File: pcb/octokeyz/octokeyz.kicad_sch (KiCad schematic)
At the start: 29 parts, among them J1 USB, J2 ISP Programming, SW1 SW_Push, SW2 SW_Push, SW3 SW_Push, SW4 SW_Push, SW5 SW_Push, SW6 SW_Push, SW7 SW_Push, SW8 SW_Push, U1 ATtiny4313-P, Y1 20MHz

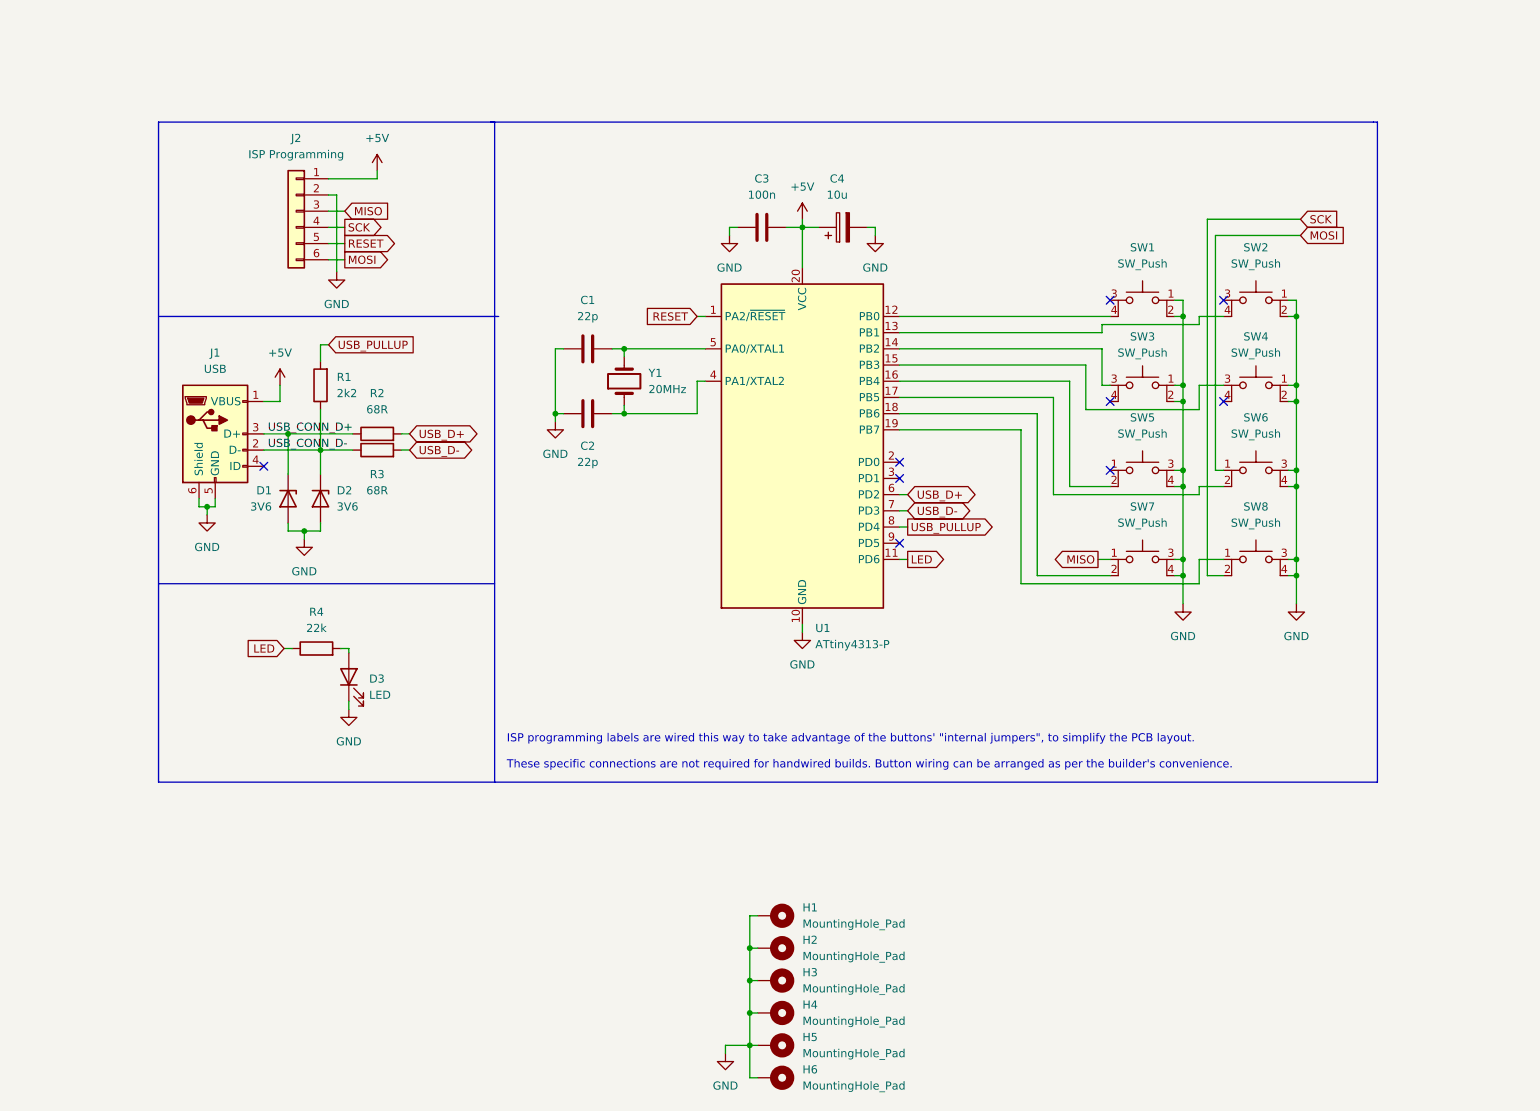
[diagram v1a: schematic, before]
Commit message: pcb: octokeyz: revision 20240616
use stm32 instead of avr microcontroller. the prices are similar
nowadays, and it will allow us to have a single DFU-capable and
BSD-licensed firmware usable by all boards.

the board outline and the position of buttons and connectors is the
same, any existing cases should still fit correctly.
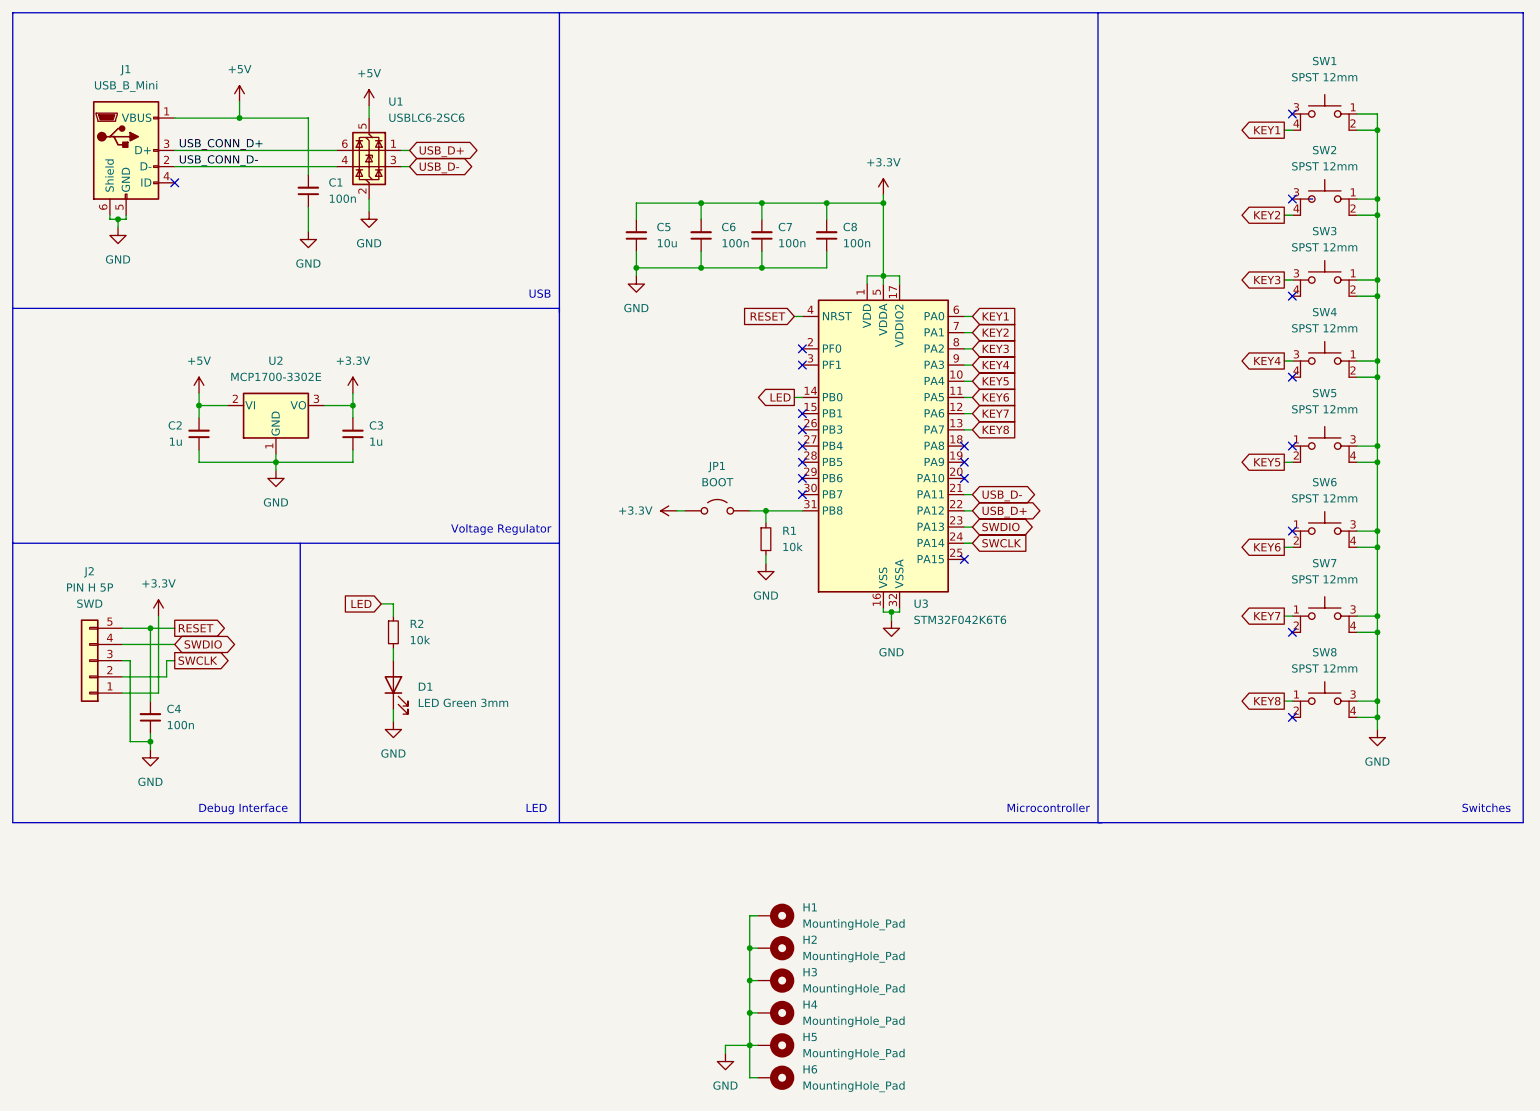
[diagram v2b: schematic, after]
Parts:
- removed C1, C2: 22p, Capacitor_THT:C_Disc_D3.0mm_W1.6mm_P2.50mm, symbol Device:C
- removed C3: 100n, octokeyz:C_TDK_FA28, symbol Device:C
- removed C4: 10u, octokeyz:CP_Radial_D5.0mm_P2.50mm_Horizontal, symbol Device:C_Polarized
- removed D1, D2: 3V6, Diode_THT:D_DO-35_SOD27_P7.62mm_Horizontal, symbol Device:D_Zener
- removed D3: LED, LED_THT:LED_D3.0mm, symbol Device:LED
- removed J2: ISP Programming, Connector_PinHeader_2.54mm:PinHeader_1x06_P2.54mm_Horizontal, symbol Connector_Generic:Conn_01x06
- removed R1: 2k2, octokeyz:R_YAGEO_MFR-25FTE52_Horizontal, symbol Device:R
- removed R2, R3: 68R, octokeyz:R_YAGEO_MFR-25FTE52_Horizontal, symbol Device:R
- removed R4: 22k, octokeyz:R_YAGEO_MFR-25FTE52_Horizontal, symbol Device:R
- removed U1: ATtiny4313-P, Package_DIP:DIP-20_W7.62mm, symbol MCU_Microchip_ATtiny:ATtiny4313-P
- removed Y1: 20MHz, Crystal:Crystal_HC49-4H_Vertical, symbol Device:Crystal
- added C1, C4, C6, C7, C8: 100n, octokeyz:C_TDK_FA28, symbol Device:C_Small
- added C2, C3: 1u, octokeyz:C_TDK_FA28, symbol Device:C_Small
- added C5: 10u, octokeyz:C_TDK_FA26, symbol Device:C_Small
- added D1: LED Green 3mm, LED_THT:LED_D3.0mm, symbol Device:LED
- added J2: PIN H 5P, Connector_PinHeader_2.54mm:PinHeader_1x05_P2.54mm_Horizontal, symbol Connector_Generic:Conn_01x05
- added JP1: BOOT, Connector_PinHeader_2.54mm:PinHeader_1x02_P2.54mm_Horizontal, symbol Jumper:Jumper_2_Open
- added R1, R2: 10k, octokeyz:R_YAGEO_MFR-25FTE52_Horizontal, symbol Device:R_Small
- added U1: USBLC6-2SC6, Package_TO_SOT_SMD:SOT-23-6, symbol Power_Protection:USBLC6-2SC6
- added U2: MCP1700-3302E, Package_TO_SOT_THT:TO-92_Inline_Wide, symbol Regulator_Linear:MCP1700x-330xxTO
- added U3: STM32F042K6T6, Package_QFP:LQFP-32_7x7mm_P0.8mm, symbol MCU_ST_STM32F0:STM32F042K6Tx
- J1: value USB -> USB_B_Mini; MPN (none) -> GMSB0522132EU
- SW1, SW2, SW3, SW4, SW5, SW6, SW7, SW8: value SW_Push -> SPST 12mm
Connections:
- net +5V: now also C1.2, C2.2, U1.5 (VBUS), U2.2 (VI)
- net GND: now also C1.1, C2.1, C3.1, C4.1, C5.1, C6.1, C7.1, C8.1, D1.1 (K), J2.3 (Pin_3), R1.2, U1.2 (GND), U2.1 (GND), U3.16 (VSS), U3.32 (VSSA)
- net LED: now also R2.1, U3.14 (PB0)
- net RESET: now also C4.2, J2.5 (Pin_5), U3.4 (NRST)
- net USB_CONN_D+: now also U1.6 (I/O1)
- net USB_CONN_D-: now also U1.4 (I/O2)
- net USB_D+: now also U1.1 (I/O1), U3.22 (PA12)
- net USB_D-: now also U1.3 (I/O2), U3.21 (PA11)
- net KEY2: now reaches SW2.4
- net KEY2: now also U3.7 (PA1)
- net KEY1: now reaches SW1.4
- net KEY1: now also U3.6 (PA0)
- net KEY3: now reaches SW3.3
- net KEY3: now also U3.8 (PA2)
- net KEY4: now reaches SW4.3
- net KEY4: now also U3.9 (PA3)
- net KEY5: now reaches SW5.2
- net KEY5: now also U3.10 (PA4)
- net KEY6: now reaches SW6.2
- net KEY6: now also U3.11 (PA5)
- net KEY8: now reaches SW8.1
- net KEY8: now also U3.13 (PA7)
- net MISO renamed KEY7
- net KEY7: now also U3.12 (PA6)
- net MOSI: no longer names the net of SW6.1
- net SCK: no longer names the net of SW8.2
- new net: JP1.1 (A), R1.1, U3.31 (PB8)
- new net: D1.2 (A), R2.2
- new net +3.3V: C3.2, C5.2, C6.2, C7.2, C8.2, J2.1 (Pin_1), JP1.2 (B), U2.3 (VO), U3.1 (VDD), U3.17 (VDDIO2), U3.5 (VDDA)
- new net SWCLK: J2.2 (Pin_2), U3.24 (PA14)
- new net SWDIO: J2.4 (Pin_4), U3.23 (PA13)
- no-connect marks 9 -> 21
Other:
- note added: "Debug Interface"
- note added: "LED"
- note added: "Microcontroller"
- note added: "Switches"
- note added: "USB"
- note added: "Voltage Regulator"
- note removed: "ISP programming labels are wired this way to take advantage of the buttons' "internal jumpers", to simplify the PCB layout. These specific connections are not required for handwired builds. Button wiring can be arranged as per the builder's convenience."
- moved on the sheet: SW1, SW2, SW3, SW4, SW5, SW6, SW7, SW8

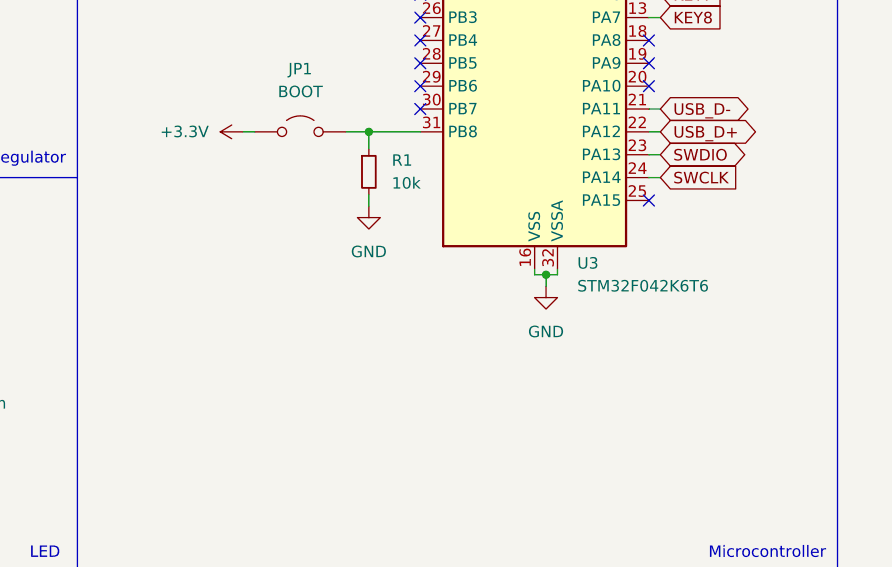
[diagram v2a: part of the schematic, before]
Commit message: pcb: added STM32F042K4T6 as microcontroller alternative
as this is a purely cosmetic change that doesn't affects the produced
boards I do not bumped revision number neither re-generated gerber
files.
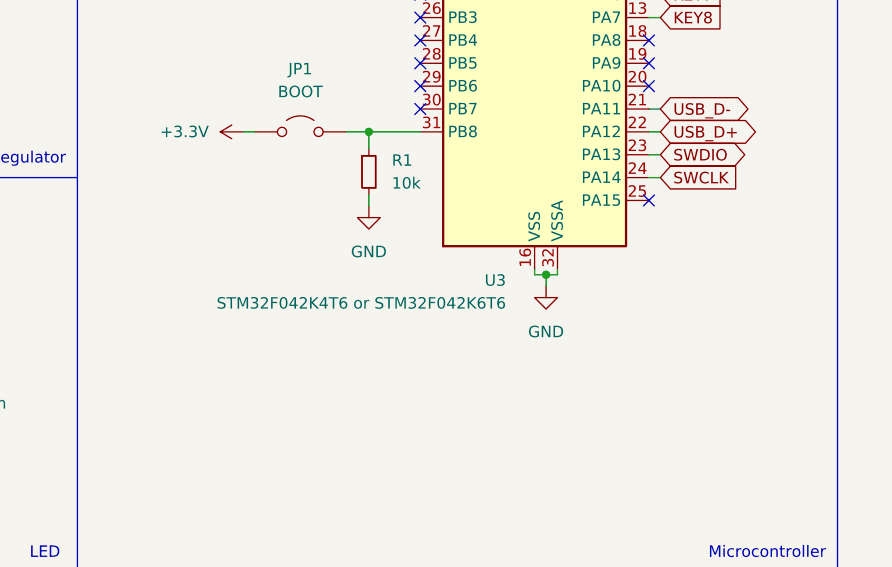
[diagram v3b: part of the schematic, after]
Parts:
- U3: value STM32F042K6T6 -> STM32F042K4T6 or STM32F042K6T6
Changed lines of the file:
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@@
 		(on_board yes)
 		(dnp no)
-		(fields_autoplaced yes)
 		(property "Reference" "U3"
-			(at 171.7391 119.38 0)
+			(at 163.83 121.285 0)
 			(effects
 				(font
 					(size 1.27 1.27)
 				)
-				(justify left)
+				(justify right)
 			)
 		)
-		(property "Value" "STM32F042K6T6"
-			(at 171.7391 121.92 0)
+		(property "Value" "STM32F042K4T6 or STM32F042K6T6"
+			(at 163.83 123.825 0)
 			(effects
 				(font
 					(size 1.27 1.27)
 				)
-				(justify left)
+				(justify right)
 			)
 		)

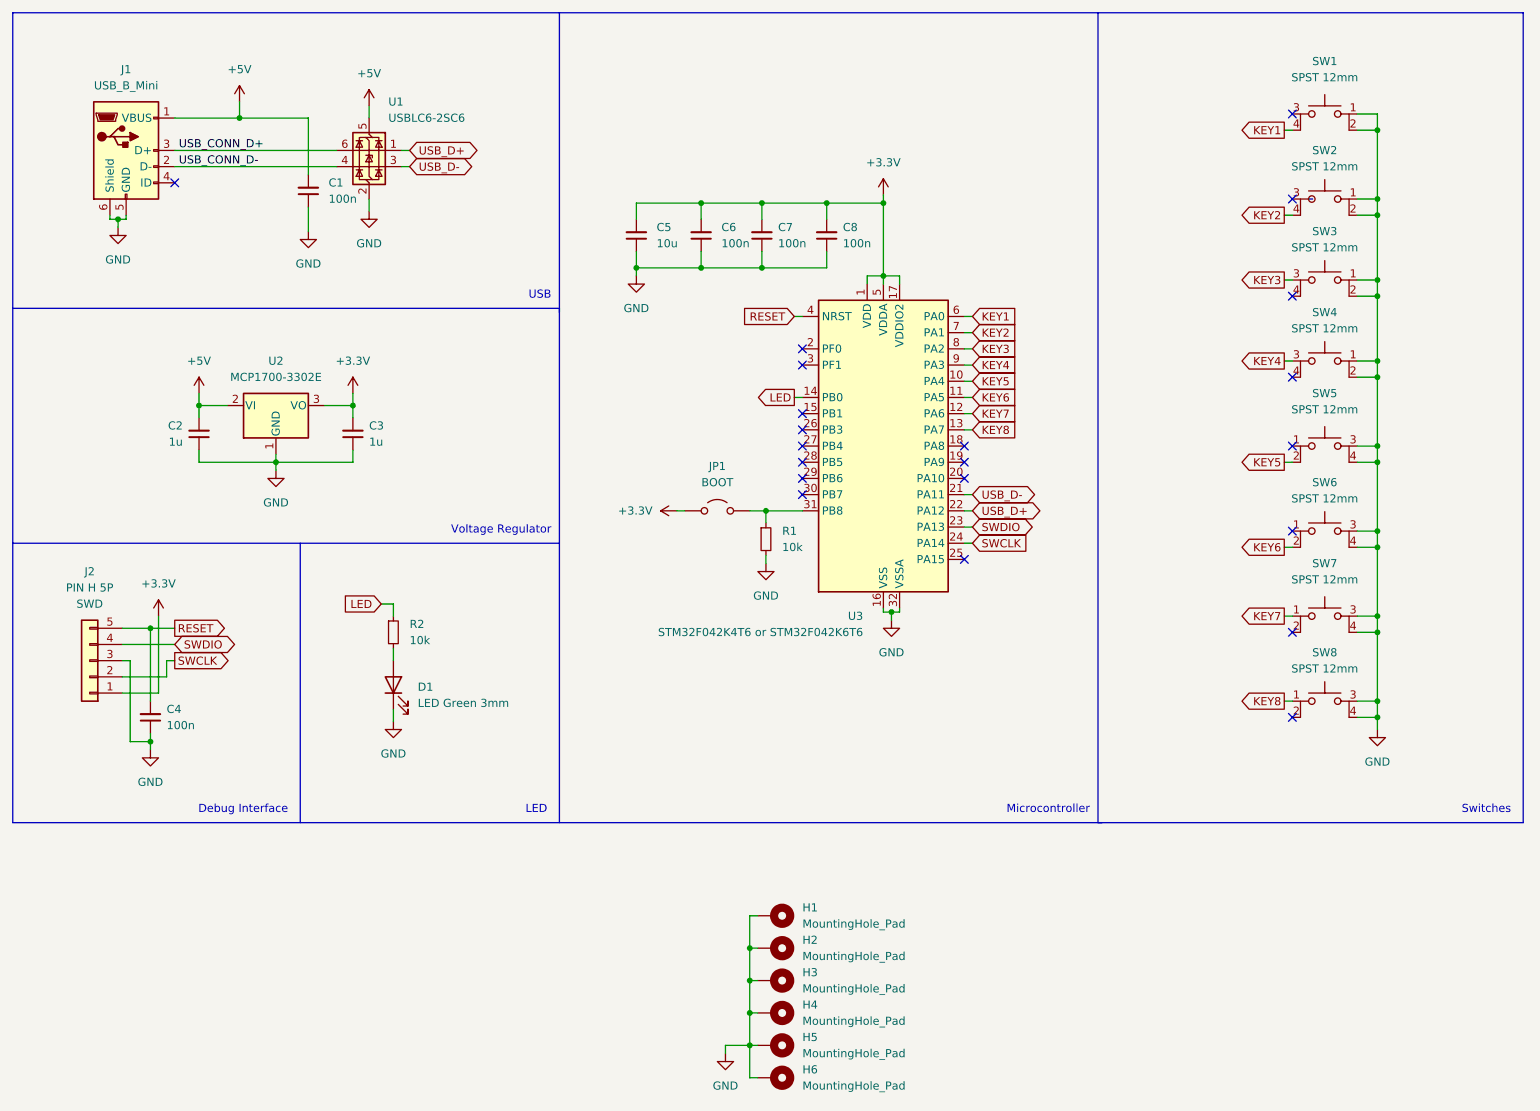
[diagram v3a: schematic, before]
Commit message: pcb: upgrade to kicad 9
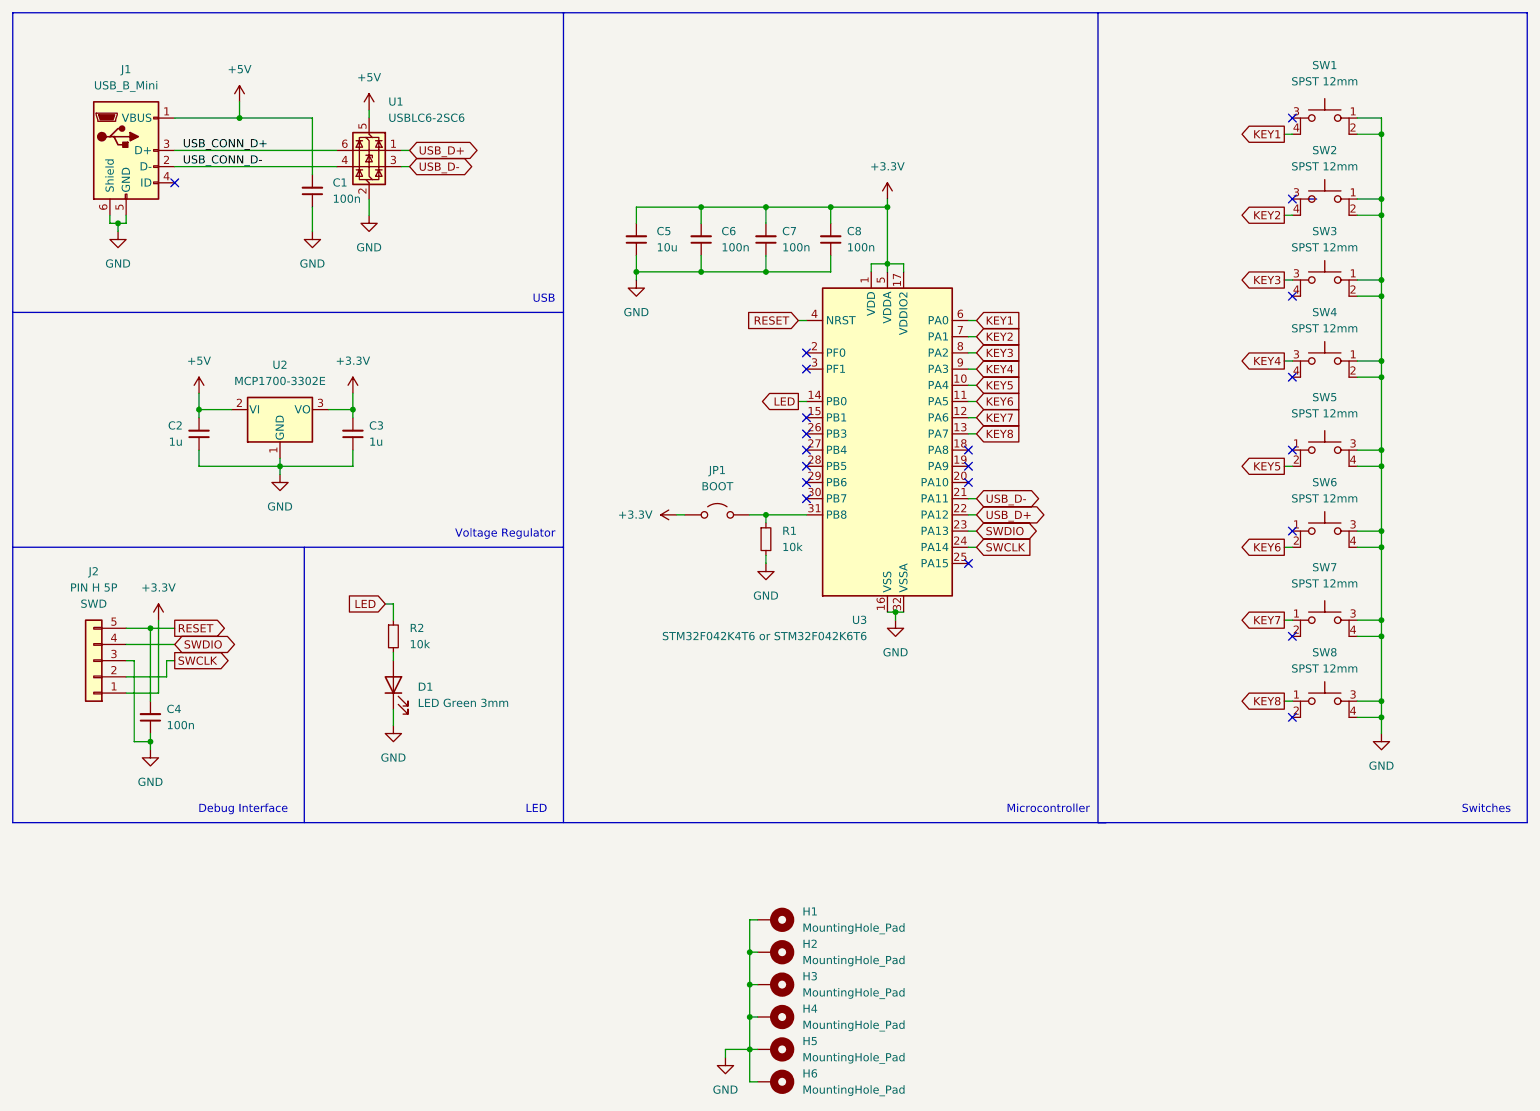
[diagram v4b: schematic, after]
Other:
- moved on the sheet: C1, C5, C6, C7, C8, H1, H2, H3, H4, H5, H6, J2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
